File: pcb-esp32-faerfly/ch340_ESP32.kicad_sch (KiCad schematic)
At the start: 9 parts, among them Q1 BC817, Q2 BC817, SW2 BOOT, SW3 EN, U4 CH340C

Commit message: added JLC part numbers
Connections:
- net at Q1.2 (E), U4.13 (~{DTR}): now also R11.2
- net at Q2.2 (E), U4.14 (~{RTS}): now also R10.2
- net at Q1.1 (B): now also R10.1
- net at R11.1: now also Q2.1 (B)
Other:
- moved on the sheet: R10, R11
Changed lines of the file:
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@@
     )
   )
-  (symbol (lib_id "000_Resistors_Immo:10k") (at 168.91 88.9 90) (unit 1)
+  (symbol (lib_id "000_Resistors_Immo:10k") (at 168.91 88.9 180) (unit 1)
     (in_bom yes) (on_board yes) (dnp no)
-    (property "Reference" "R10" (at 168.91 86.36 90)
+    (property "Reference" "R10" (at 168.275 86.36 0)
       (effects (font (size 1.27 1.27)))
     )
-    (property "Value" "10k" (at 168.91 91.44 90)
+    (property "Value" "10k" (at 169.545 90.805 0)
       (effects (font (size 1.27 1.27)))
     )
-    (property "Footprint" "Resistor_SMD:R_0805_2012Metric_Pad1.20x1.40mm_HandSolder" (at 170.688 88.9 0)
+    (property "Footprint" "Resistor_SMD:R_0805_2012Metric_Pad1.20x1.40mm_HandSolder" (at 168.91 87.122 0)
       (effects (font (size 1.27 1.27)) hide)
     )
@@
       (effects (font (size 1.27 1.27)) hide)
     )
-    (property "JLCpart" "C2930231" (at 171.45 87.63 0)
+    (property "JLCpart" "C2930231" (at 167.64 86.36 0)
       (effects (font (size 1.27 1.27)) hide)
     )
-    (property "Cost" "0.002" (at 171.45 88.9 0)
+    (property "Cost" "0.002" (at 168.91 86.36 0)
       (effects (font (size 1.27 1.27)) hide)
     )
@@
     )
   )
-  (symbol (lib_id "000_Resistors_Immo:10k") (at 168.91 104.14 90) (unit 1)
+  (symbol (lib_id "000_Resistors_Immo:10k") (at 168.91 104.14 180) (unit 1)
     (in_bom yes) (on_board yes) (dnp no)
-    (property "Reference" "R11" (at 168.91 101.6 90)
+    (property "Reference" "R11" (at 167.64 101.6 0)
       (effects (font (size 1.27 1.27)))
     )
-    (property "Value" "10k" (at 168.91 106.68 90)
+    (property "Value" "10k" (at 170.815 106.68 0)
       (effects (font (size 1.27 1.27)))
     )
-    (property "Footprint" "Resistor_SMD:R_0805_2012Metric_Pad1.20x1.40mm_HandSolder" (at 170.688 104.14 0)
+    (property "Footprint" "Resistor_SMD:R_0805_2012Metric_Pad1.20x1.40mm_HandSolder" (at 168.91 102.362 0)
       (effects (font (size 1.27 1.27)) hide)
     )
@@
       (effects (font (size 1.27 1.27)) hide)
     )
-    (property "JLCpart" "C2930231" (at 171.45 102.87 0)
+    (property "JLCpart" "C2930231" (at 167.64 101.6 0)
       (effects (font (size 1.27 1.27)) hide)
     )
-    (property "Cost" "0.002" (at 171.45 104.14 0)
+    (property "Cost" "0.002" (at 168.91 101.6 0)
       (effects (font (size 1.27 1.27)) hide)
     )

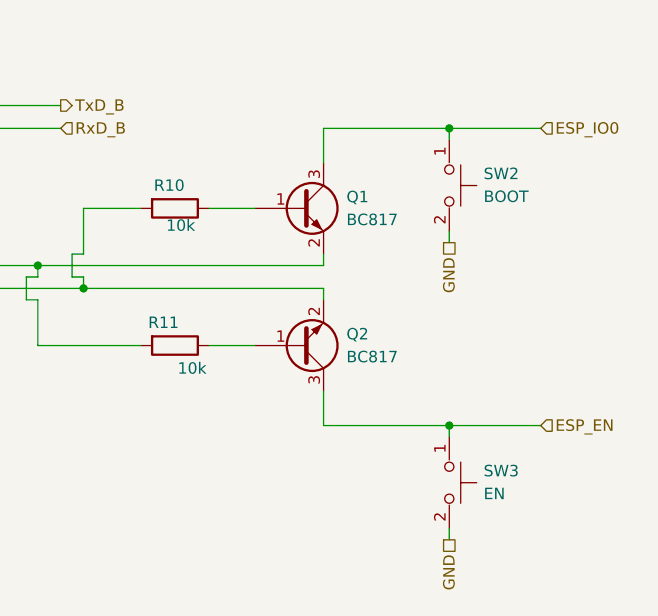
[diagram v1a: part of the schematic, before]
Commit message: Added Complete BOM
Ready for Parts Shopping!
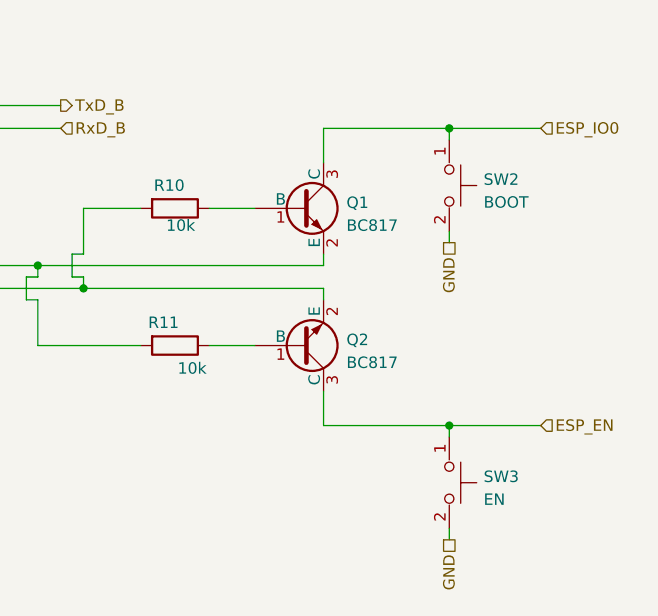
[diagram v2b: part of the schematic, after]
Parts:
- Q1, Q2: symbol Transistor_BJT:BC817 -> 000_Transistors_BJT_Immo:BC817; Cost (none) -> 0.0225; JLCpart (none) -> C2137
- SW2, SW3: footprint Button_Switch_SMD:SW_SPST_EVQPE1 -> 000_Switches_Immo:SW_SPST_EVQPE1; Cost (none) -> 0.3052; JLCpart (none) -> C699451
- U4: symbol Interface_USB:CH340C -> 000_IC_immo:CH340C; Cost (none) -> 0.4725; JLCpart (none) -> C84681
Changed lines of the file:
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@@
     )
   )
-  (symbol (lib_id "Interface_USB:CH340C") (at 135.89 87.63 0) (unit 1)
+  (symbol (lib_id "000_IC_immo:CH340C") (at 135.89 87.63 0) (unit 1)
     (in_bom yes) (on_board yes) (dnp no) (fields_autoplaced)
     (property "Reference" "U4" (at 135.3694 102.87 0)
@@
     )
     (property "Datasheet" "https://datasheet.lcsc.com/szlcsc/Jiangsu-Qin-Heng-CH340C_C84681.pdf" (at 127 67.31 0)
+      (effects (font (size 1.27 1.27)) hide)
+    )
+    (property "JLCpart" "C84681" (at 135.89 87.63 0)
+      (effects (font (size 1.27 1.27)) hide)
+    )
+    (property "Cost" "0.4725" (at 135.89 87.63 0)
       (effects (font (size 1.27 1.27)) hide)
     )
@@
     )
   )
-  (symbol (lib_id "Transistor_BJT:BC817") (at 182.88 88.9 0) (unit 1)
-    (in_bom yes) (on_board yes) (dnp no) (fields_autoplaced)
-    (property "Reference" "Q1" (at 187.96 87.6299 0)
-      (effects (font (size 1.27 1.27)) (justify left))
-    )
-    (property "Value" "BC817" (at 187.96 90.1699 0)
-      (effects (font (size 1.27 1.27)) (justify left))
-    )
-    (property "Footprint" "Package_TO_SOT_SMD:SOT-23" (at 187.96 90.805 0)
+  (symbol (lib_id "000_Transistors_BJT_Immo:BC817") (at 182.88 88.9 0) (unit 1)
+    (in_bom yes) (on_board yes) (dnp no) (fields_autoplaced)
+    (property "Reference" "Q1" (at 187.96 88.265 0)
+      (effects (font (size 1.27 1.27)) (justify left))
+    )
+    (property "Value" "BC817" (at 187.96 90.805 0)
+      (effects (font (size 1.27 1.27)) (justify left))
+    )
+    (property "Footprint" "Package_TO_SOT_SMD:SOT-23" (at 195.58 103.505 0)
       (effects (font (size 1.27 1.27) italic) (justify left) hide)
     )
-    (property "Datasheet" "https://www.onsemi.com/pub/Collateral/BC818-D.pdf" (at 182.88 88.9 0)
-      (effects (font (size 1.27 1.27)) (justify left) hide)
+    (property "Datasheet" "https://www.onsemi.com/pub/Collateral/BC818-D.pdf" (at 190.5 101.6 0)
+      (effects (font (size 1.27 1.27)) (justify left) hide)
+    )
+    (property "Sim.Pins" "1=1 2=2 3=3" (at 182.88 88.9 0)
+      (effects (font (size 0 0)) hide)
+    )
+    (property "Sim.Device" "SPICE" (at 195.58 83.82 0)
+      (effects (font (size 1.27 1.27)) (justify left) hide)
+    )
+    (property "Sim.Params" "type=\"Q\" model=\"BC817\" lib=\"spice-models\\BC817.lib\"" (at 182.88 88.9 0)
+      (effects (font (size 0 0)) hide)
+    )
+    (property "JLCpart" "C2137" (at 182.88 88.9 0)
+      (effects (font (size 1.27 1.27)) hide)
+    )
+    (property "Cost" "0.0225" (at 182.88 88.9 0)
+      (effects (font (size 1.27 1.27)) hide)
     )
     (pin "1")
@@
   (symbol (lib_id "000_Switches_Immo:pushbutton_tactile_2pin_SMD") (at 196.85 119.38 270) (unit 1)
     (in_bom yes) (on_board yes) (dnp no) (fields_autoplaced)
-    (property "Reference" "SW3" (at 203.2 118.0799 90)
-      (effects (font (size 1.27 1.27)) (justify left))
-    )
-    (property "Value" "EN" (at 203.2 120.6199 90)
-      (effects (font (size 1.27 1.27)) (justify left))
-    )
-    (property "Footprint" "Button_Switch_SMD:SW_SPST_EVQPE1" (at 204.47 119.38 0)
+    (property "Reference" "SW3" (at 203.2 118.715 90)
+      (effects (font (size 1.27 1.27)) (justify left))
+    )
+    (property "Value" "EN" (at 203.2 121.255 90)
+      (effects (font (size 1.27 1.27)) (justify left))
+    )
+    (property "Footprint" "000_Switches_Immo:SW_SPST_EVQPE1" (at 204.47 119.38 0)
       (effects (font (size 1.27 1.27)) hide)
     )
     (property "Datasheet" "" (at 204.47 119.38 0)
+      (effects (font (size 1.27 1.27)) hide)
+    )
+    (property "JLCpart" "C699451" (at 196.85 119.38 0)
+      (effects (font (size 1.27 1.27)) hide)
+    )
+    (property "Cost" "0.3052" (at 196.85 119.38 0)
       (effects (font (size 1.27 1.27)) hide)
     )
@@
   (symbol (lib_id "000_Switches_Immo:pushbutton_tactile_2pin_SMD") (at 196.85 86.36 270) (unit 1)
     (in_bom yes) (on_board yes) (dnp no) (fields_autoplaced)
-    (property "Reference" "SW2" (at 203.2 85.0599 90)
-      (effects (font (size 1.27 1.27)) (justify left))
-    )
-    (property "Value" "BOOT" (at 203.2 87.5999 90)
-      (effects (font (size 1.27 1.27)) (justify left))
-    )
-    (property "Footprint" "Button_Switch_SMD:SW_SPST_EVQPE1" (at 204.47 86.36 0)
+    (property "Reference" "SW2" (at 203.2 85.695 90)
+      (effects (font (size 1.27 1.27)) (justify left))
+    )
+    (property "Value" "BOOT" (at 203.2 88.235 90)
+      (effects (font (size 1.27 1.27)) (justify left))
+    )
+    (property "Footprint" "000_Switches_Immo:SW_SPST_EVQPE1" (at 204.47 86.36 0)
       (effects (font (size 1.27 1.27)) hide)
     )
@@
       (effects (font (size 1.27 1.27)) hide)
     )
+    (property "JLCpart" "C699451" (at 196.85 86.36 0)
+      (effects (font (size 1.27 1.27)) hide)
+    )
+    (property "Cost" "0.3052" (at 196.85 86.36 0)
+      (effects (font (size 1.27 1.27)) hide)
+    )
     (pin "1")
     (pin "2")
@@
     )
   )
-  (symbol (lib_id "Transistor_BJT:BC817") (at 182.88 104.14 0) (mirror x) (unit 1)
-    (in_bom yes) (on_board yes) (dnp no) (fields_autoplaced)
-    (property "Reference" "Q2" (at 187.96 102.8699 0)
-      (effects (font (size 1.27 1.27)) (justify left))
-    )
-    (property "Value" "BC817" (at 187.96 105.4099 0)
-      (effects (font (size 1.27 1.27)) (justify left))
-    )
-    (property "Footprint" "Package_TO_SOT_SMD:SOT-23" (at 187.96 102.235 0)
+  (symbol (lib_id "000_Transistors_BJT_Immo:BC817") (at 182.88 104.14 0) (mirror x) (unit 1)
+    (in_bom yes) (on_board yes) (dnp no) (fields_autoplaced)
+    (property "Reference" "Q2" (at 187.96 103.505 0)
+      (effects (font (size 1.27 1.27)) (justify left))
+    )
+    (property "Value" "BC817" (at 187.96 106.045 0)
+      (effects (font (size 1.27 1.27)) (justify left))
+    )
+    (property "Footprint" "Package_TO_SOT_SMD:SOT-23" (at 195.58 89.535 0)
       (effects (font (size 1.27 1.27) italic) (justify left) hide)
     )
-    (property "Datasheet" "https://www.onsemi.com/pub/Collateral/BC818-D.pdf" (at 182.88 104.14 0)
-      (effects (font (size 1.27 1.27)) (justify left) hide)
-    )
-    (pin "1")
+    (property "Datasheet" "https://www.onsemi.com/pub/Collateral/BC818-D.pdf" (at 190.5 91.44 0)
+      (effects (font (size 1.27 1.27)) (justify left) hide)
+    )
+    (property "Sim.Pins" "1=1 2=2 3=3" (at 182.88 104.14 0)
+      (effects (font (size 0 0)) hide)
+    )
+    (property "Sim.Device" "SPICE" (at 195.58 109.22 0)
+      (effects (font (size 1.27 1.27)) (justify left) hide)
+    )
+    (property "Sim.Params" "type=\"Q\" model=\"BC817\" lib=\"spice-models\\BC817.lib\"" (at 182.88 104.14 0)
+      (effects (font (size 0 0)) hide)
+    )
+    (property "JLCpart" "C2137" (at 182.88 104.14 0)
+      (effects (font (size 1.27 1.27)) hide)
+    )
+    (property "Cost" "0.0225" (at 182.88 104.14 0)
+      (effects (font (size 1.27 1.27)) hide)
+    )
+    (pin "1")
